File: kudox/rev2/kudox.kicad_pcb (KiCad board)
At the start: 2 copper layers, 143.6 x 129.5 mm, 83 parts, among them K0 KEYSW, K1 KEYSW, K10 KEYSW, K11 KEYSW, K12 KEYSW, K13 KEYSW, K14 KEYSW, K15 KEYSW, K16 KEYSW, K2 KEYSW, K20 KEYSW, K21 KEYSW, K22 KEYSW, K23 KEYSW, K24 KEYSW, K25 KEYSW, K3 KEYSW, K30 KEYSW, K31 KEYSW, K32 KEYSW, K33 KEYSW, K34 KEYSW, K35 KEYSW, K4 KEYSW, K40 KEYSW, K41 KEYSW, K42 KEYSW, K43 KEYSW, K44 KEYSW, K45 KEYSW, K46 KEYSW, K5 KEYSW, K6 KEYSW, U1 ProMicro

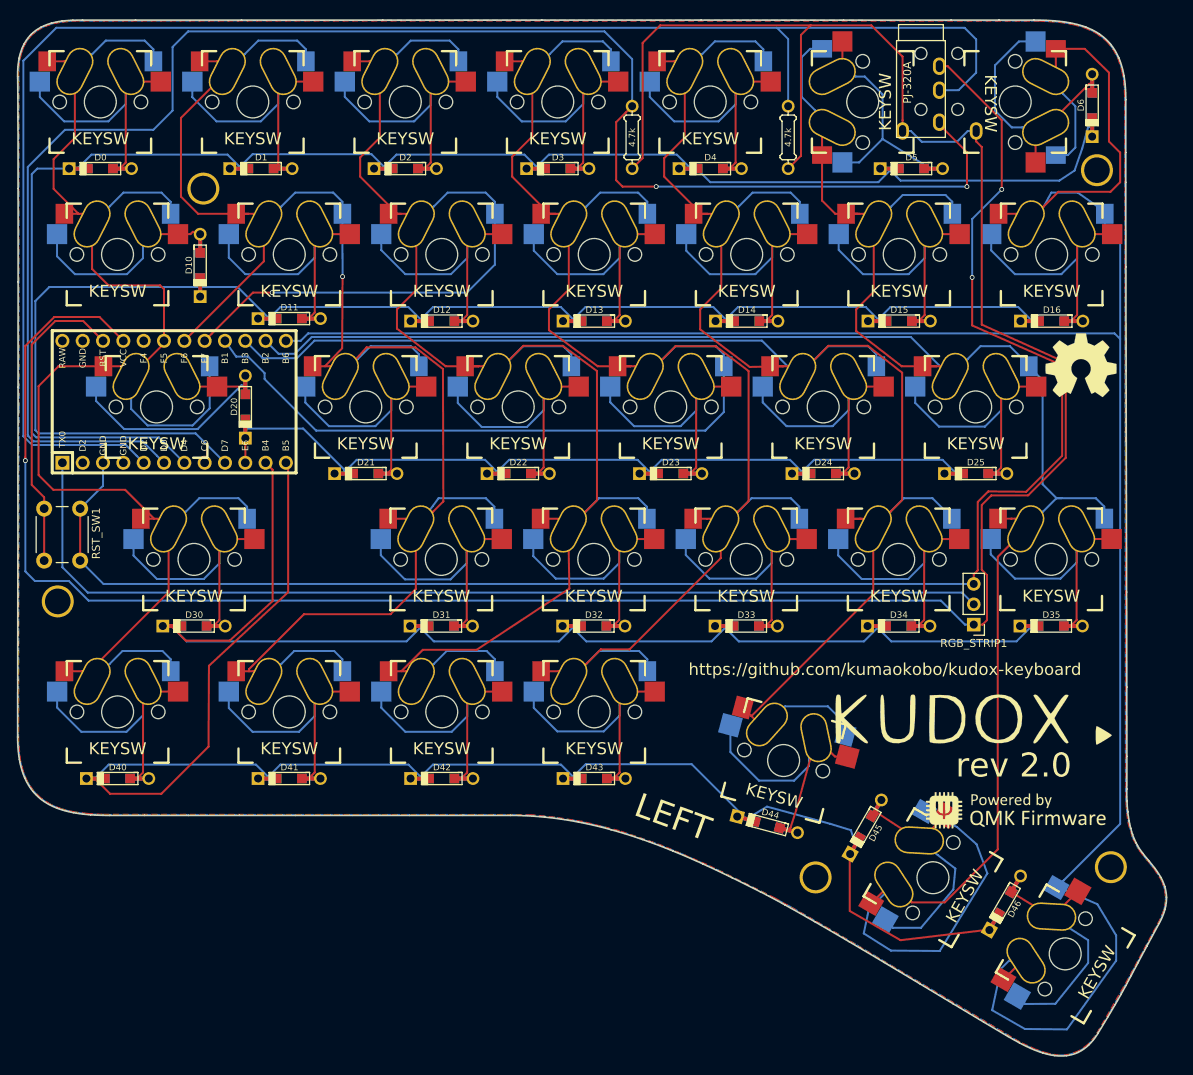
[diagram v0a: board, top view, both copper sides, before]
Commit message: Modified positions of holes.
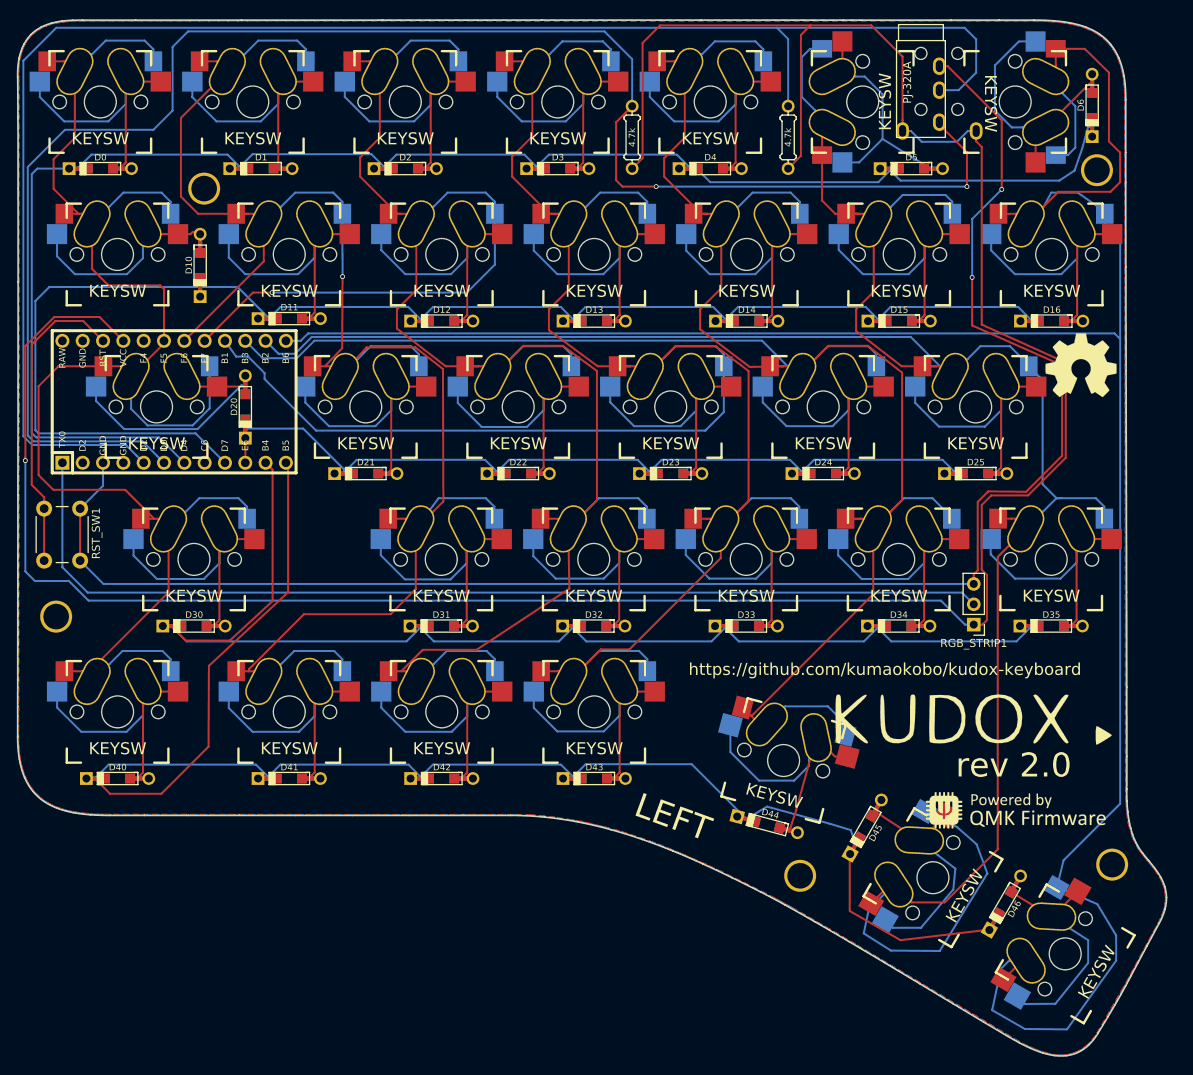
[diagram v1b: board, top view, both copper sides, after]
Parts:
- moved HOLE_M3 1.94 mm to (178.0, 138.4)
- moved HOLE_M3 1.91 mm to (85.0, 106.0)
- moved HOLE_M3 0.36 mm to (217.0, 137.0)
- moved HOLE_M3 0.10 mm to (103.5, 52.5)
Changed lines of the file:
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@@
     (thickness 1.6)
     (drawings 143)
-    (tracks 1082)
+    (tracks 1083)
     (zones 0)
     (modules 83)
@@
   )
   (module keyboard_parts:HOLE_M3 (layer F.Cu)
-    (at 179.93 138.56)
+    (at 178 138.36)
     (fp_text reference HOLE_M3 (at 0 -4.5) (layer F.SilkS) hide
       (effects (font (size 1.524 1.524) (thickness 0.3048)))
@@
   )
   (module keyboard_parts:HOLE_M3 (layer F.Cu)
-    (at 216.84 137.28)
+    (at 217 136.96)
     (fp_text reference HOLE_M3 (at 0 -4.5) (layer F.SilkS) hide
       (effects (font (size 1.524 1.524) (thickness 0.3048)))
@@
   )
   (module keyboard_parts:HOLE_M3 (layer F.Cu)
-    (at 103.4 52.46)
+    (at 103.5 52.46)
     (fp_text reference HOLE_M3 (at 0 -4.5) (layer F.SilkS) hide
       (effects (font (size 1.524 1.524) (thickness 0.3048)))
@@
   )
   (module keyboard_parts:HOLE_M3 (layer F.Cu)
-    (at 85.2 104.06)
+    (at 85 105.96)
     (fp_text reference HOLE_M3 (at -0.1 3.8) (layer F.SilkS) hide
       (effects (font (size 1.524 1.524) (thickness 0.3048)))
@@
   (gr_line (start 210.7 160.94) (end 237.7 160.94) (layer Dwgs.User) (width 0.1))
   (gr_line (start 60 31.36) (end 95 31.36) (layer Dwgs.User) (width 0.1))
-  (gr_line (start 59.99 130.84) (end 94.99 130.84) (layer Dwgs.User) (width 0.15))
+  (gr_line (start 59.99 130.84) (end 94.99 130.84) (layer Dwgs.User) (width 0.1))
   (gr_line (start 80.1 20.96) (end 80.1 165.86) (layer Dwgs.User) (width 0.1))
   (gr_line (start 223.85 21.04) (end 223.85 165.94) (layer Dwgs.User) (width 0.1))
@@
     (effects (font (size 3 3) (thickness 0.3)))
   )
-  (gr_curve (pts (xy 103.3398 50.856665) (xy 104.275584 50.856665) (xy 105.034187 51.615268) (xy 105.034187 52.551052)) (layer Eco1.User) (width 0.2))
+  (gr_curve (pts (xy 103.5098 50.766665) (xy 104.445584 50.766665) (xy 105.204187 51.525268) (xy 105.204187 52.461052)) (layer Eco1.User) (width 0.2))
   (gr_curve (pts (xy 213.413283 50.161035) (xy 213.413283 49.225251) (xy 214.171888 48.466648) (xy 215.107667 48.466648)) (layer Eco1.User) (width 0.2))
-  (gr_curve (pts (xy 85.195614 102.415616) (xy 86.131398 102.415616) (xy 86.89 103.174221) (xy 86.89 104.11)) (layer Eco1.User) (width 0.2))
-  (gr_curve (pts (xy 178.198782 138.530273) (xy 178.198782 137.594494) (xy 178.957386 136.835889) (xy 179.893166 136.835889)) (layer Eco1.User) (width 0.2))
-  (gr_curve (pts (xy 179.893166 140.224657) (xy 178.957386 140.224657) (xy 178.198782 139.466053) (xy 178.198782 138.530273)) (layer Eco1.User) (width 0.2))
-  (gr_curve (pts (xy 181.58755 138.530273) (xy 181.58755 139.466053) (xy 180.828945 140.224657) (xy 179.893166 140.224657)) (layer Eco1.User) (width 0.2))
-  (gr_curve (pts (xy 179.893166 136.835889) (xy 180.828945 136.835889) (xy 181.58755 137.594494) (xy 181.58755 138.530273)) (layer Eco1.User) (width 0.2))
-  (gr_curve (pts (xy 101.645414 52.551052) (xy 101.645414 51.615268) (xy 102.404017 50.856665) (xy 103.3398 50.856665)) (layer Eco1.User) (width 0.2))
-  (gr_curve (pts (xy 103.3398 54.245439) (xy 102.404017 54.245439) (xy 101.645414 53.486836) (xy 101.645414 52.551052)) (layer Eco1.User) (width 0.2))
-  (gr_curve (pts (xy 105.034187 52.551052) (xy 105.034187 53.486836) (xy 104.275584 54.245439) (xy 103.3398 54.245439)) (layer Eco1.User) (width 0.2))
+  (gr_curve (pts (xy 85.005614 104.265616) (xy 85.941398 104.265616) (xy 86.7 105.024221) (xy 86.7 105.96)) (layer Eco1.User) (width 0.2))
+  (gr_curve (pts (xy 176.298782 138.360273) (xy 176.298782 137.424494) (xy 177.057386 136.665889) (xy 177.993166 136.665889)) (layer Eco1.User) (width 0.2))
+  (gr_curve (pts (xy 177.993166 140.054657) (xy 177.057386 140.054657) (xy 176.298782 139.296053) (xy 176.298782 138.360273)) (layer Eco1.User) (width 0.2))
+  (gr_curve (pts (xy 179.68755 138.360273) (xy 179.68755 139.296053) (xy 178.928945 140.054657) (xy 177.993166 140.054657)) (layer Eco1.User) (width 0.2))
+  (gr_curve (pts (xy 177.993166 136.665889) (xy 178.928945 136.665889) (xy 179.68755 137.424494) (xy 179.68755 138.360273)) (layer Eco1.User) (width 0.2))
+  (gr_curve (pts (xy 101.815414 52.461052) (xy 101.815414 51.525268) (xy 102.574017 50.766665) (xy 103.5098 50.766665)) (layer Eco1.User) (width 0.2))
+  (gr_curve (pts (xy 103.5098 54.155439) (xy 102.574017 54.155439) (xy 101.815414 53.396836) (xy 101.815414 52.461052)) (layer Eco1.User) (width 0.2))
+  (gr_curve (pts (xy 105.204187 52.461052) (xy 105.204187 53.396836) (xy 104.445584 54.155439) (xy 103.5098 54.155439)) (layer Eco1.User) (width 0.2))
   (gr_curve (pts (xy 215.107667 51.855422) (xy 214.171888 51.855422) (xy 213.413283 51.096819) (xy 213.413283 50.161035)) (layer Eco1.User) (width 0.2))
   (gr_curve (pts (xy 216.802051 50.161035) (xy 216.802051 51.096819) (xy 216.043447 51.855422) (xy 215.107667 51.855422)) (layer Eco1.User) (width 0.2))
   (gr_curve (pts (xy 215.107667 48.466648) (xy 216.043447 48.466648) (xy 216.802051 49.225251) (xy 216.802051 50.161035)) (layer Eco1.User) (width 0.2))
-  (gr_curve (pts (xy 215.103649 137.155215) (xy 215.103649 136.219435) (xy 215.862253 135.460831) (xy 216.798033 135.460831)) (layer Eco1.User) (width 0.2))
-  (gr_curve (pts (xy 216.798033 138.849599) (xy 215.862253 138.849599) (xy 215.103649 138.090994) (xy 215.103649 137.155215)) (layer Eco1.User) (width 0.2))
-  (gr_curve (pts (xy 218.492417 137.155215) (xy 218.492417 138.090994) (xy 217.733812 138.849599) (xy 216.798033 138.849599)) (layer Eco1.User) (width 0.2))
-  (gr_curve (pts (xy 216.798033 135.460831) (xy 217.733812 135.460831) (xy 218.492417 136.219435) (xy 218.492417 137.155215)) (layer Eco1.User) (width 0.2))
-  (gr_curve (pts (xy 83.501227 104.11) (xy 83.501227 103.174221) (xy 84.259829 102.415616) (xy 85.195614 102.415616)) (layer Eco1.User) (width 0.2))
-  (gr_curve (pts (xy 85.195614 105.804384) (xy 84.259829 105.804384) (xy 83.501227 105.045779) (xy 83.501227 104.11)) (layer Eco1.User) (width 0.2))
-  (gr_curve (pts (xy 86.89 104.11) (xy 86.89 105.045779) (xy 86.131398 105.804384) (xy 85.195614 105.804384)) (layer Eco1.User) (width 0.2))
+  (gr_curve (pts (xy 215.303649 136.955215) (xy 215.303649 136.019435) (xy 216.062253 135.260831) (xy 216.998033 135.260831)) (layer Eco1.User) (width 0.2))
+  (gr_curve (pts (xy 216.998033 138.649599) (xy 216.062253 138.649599) (xy 215.303649 137.890994) (xy 215.303649 136.955215)) (layer Eco1.User) (width 0.2))
+  (gr_curve (pts (xy 218.692417 136.955215) (xy 218.692417 137.890994) (xy 217.933812 138.649599) (xy 216.998033 138.649599)) (layer Eco1.User) (width 0.2))
+  (gr_curve (pts (xy 216.998033 135.260831) (xy 217.933812 135.260831) (xy 218.692417 136.019435) (xy 218.692417 136.955215)) (layer Eco1.User) (width 0.2))
+  (gr_curve (pts (xy 83.311227 105.96) (xy 83.311227 105.024221) (xy 84.069829 104.265616) (xy 85.005614 104.265616)) (layer Eco1.User) (width 0.2))
+  (gr_curve (pts (xy 85.005614 107.654384) (xy 84.069829 107.654384) (xy 83.311227 106.895779) (xy 83.311227 105.96)) (layer Eco1.User) (width 0.2))
+  (gr_curve (pts (xy 86.7 105.96) (xy 86.7 106.895779) (xy 85.941398 107.654384) (xy 85.005614 107.654384)) (layer Eco1.User) (width 0.2))
   (gr_curve (pts (xy 87.095678 31.415371) (xy 87.524801 31.400242) (xy 87.933036 31.399453) (xy 88.305313 31.399453)) (layer Edge.Cuts) (width 0.2))
   (gr_curve (pts (xy 85.760717 31.517332) (xy 86.216544 31.45997) (xy 86.666555 31.430501) (xy 87.095678 31.415371)) (layer Edge.Cuts) (width 0.2))
@@
   (segment (start 216.08 57.11) (end 218 59.03) (width 0.25) (layer B.Cu) (net 44))
   (segment (start 216.08 55.61) (end 216.08 57.11) (width 0.25) (layer B.Cu) (net 44))
-  (segment (start 210.926556 138.953626) (end 210.050591 139.829591) (width 0.25) (layer B.Cu) (net 44))
-  (segment (start 218 131.880182) (end 210.926556 138.953626) (width 0.25) (layer B.Cu) (net 44))
   (segment (start 209.4 52.96) (end 208.438359 54.701641) (width 0.25) (layer B.Cu) (net 44))
   (segment (start 212.7 52.96) (end 209.4 52.96) (width 0.25) (layer B.Cu) (net 44))
@@
   (segment (start 212.4 47.33) (end 212.4 42.16) (width 0.25) (layer B.Cu) (net 44))
   (segment (start 209.96 48.27) (end 211.46 48.27) (width 0.25) (layer B.Cu) (net 44))
-  (segment (start 218 71.26) (end 218 131.880182) (width 0.25) (layer B.Cu) (net 44))
   (segment (start 218 59.03) (end 218 71.26) (width 0.25) (layer B.Cu) (net 44))
   (segment (start 217.3 70.56) (end 218 71.26) (width 0.25) (layer B.Cu) (net 44))
@@
   (segment (start 216.6 37.96) (end 216.6 46.56) (width 0.25) (layer F.Cu) (net 44))
   (segment (start 209.96 34.99) (end 213.58 34.99) (width 0.25) (layer F.Cu) (net 44))
+  (segment (start 210.3 138.96) (end 210.050591 139.829591) (width 0.25) (layer B.Cu) (net 44))
+  (segment (start 210.926556 136.433444) (end 210.3 138.96) (width 0.25) (layer B.Cu) (net 44))
+  (segment (start 218 129.36) (end 210.926556 136.433444) (width 0.25) (layer B.Cu) (net 44))
+  (segment (start 218 71.26) (end 218 129.36) (width 0.25) (layer B.Cu) (net 44))
   (segment (start 200.8 106.96) (end 199.7 106.96) (width 0.25) (layer F.Cu) (net 45))
   (segment (start 201.35 106.41) (end 200.8 106.96) (width 0.25) (layer F.Cu) (net 45))

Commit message: Modified drill aux.
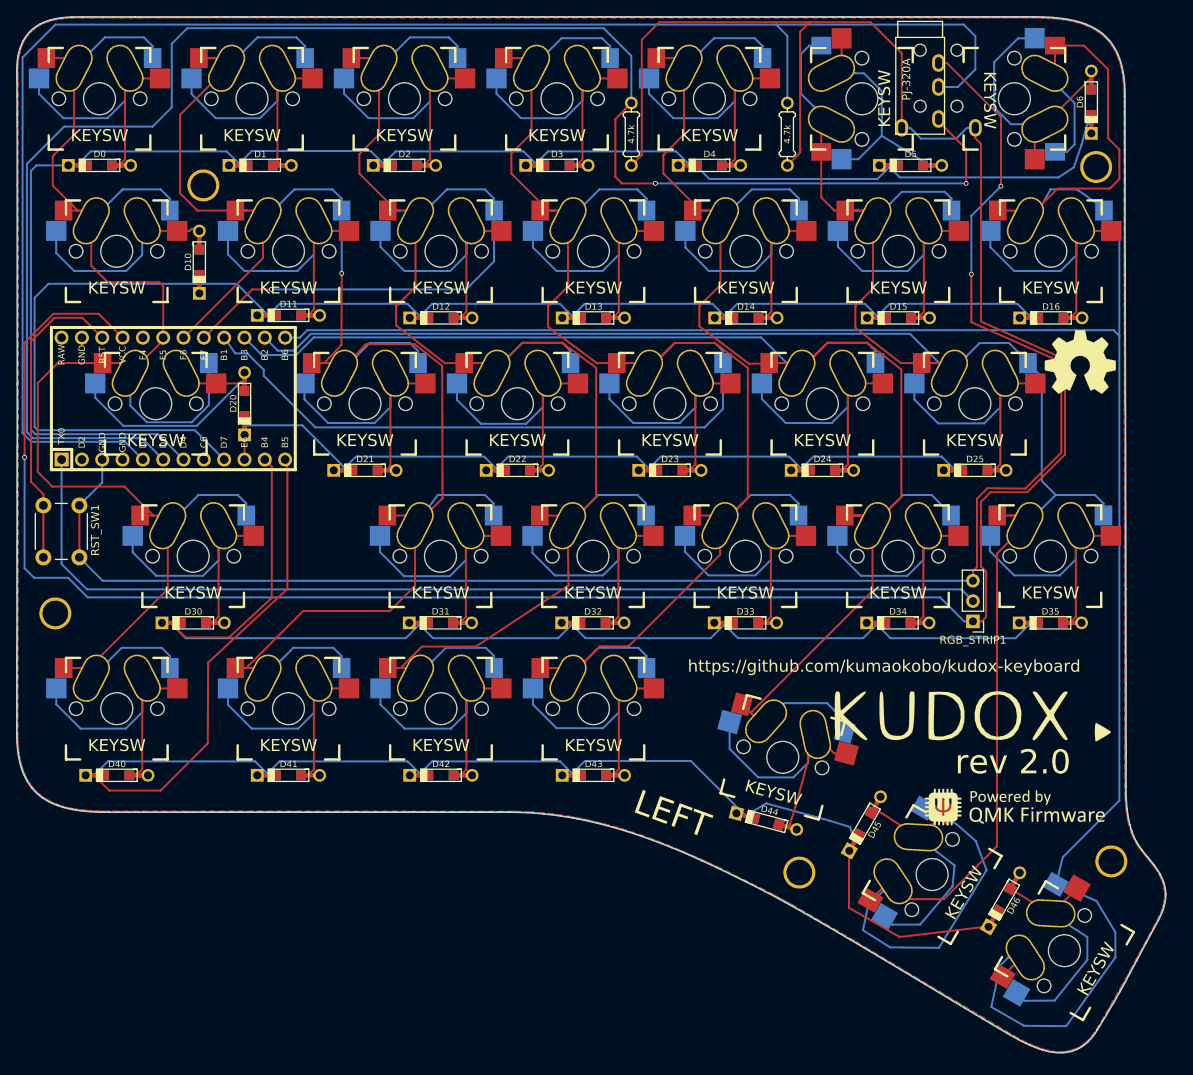
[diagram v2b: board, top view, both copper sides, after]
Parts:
- moved G*** 0.41 mm to (198.7, 118.5)
- moved D20 0.41 mm to (108.5, 79.3)
- moved D30 0.41 mm to (102.1, 106.7)
- moved D40 0.41 mm to (92.6, 125.8)
- moved K21 0.41 mm to (123.6, 79.3)
- moved K30 0.41 mm to (102.1, 98.4)
- moved K40 0.41 mm to (92.6, 117.5)
- moved -3 0.41 mm to (213.0, 74.2)
- moved D10 0.41 mm to (102.9, 61.7)
- moved D31 0.41 mm to (133.0, 106.7)
- moved D32 0.41 mm to (152.1, 106.7)
- moved D33 0.41 mm to (171.2, 106.7)
- moved D34 0.41 mm to (190.2, 106.7)
- moved D35 0.41 mm to (209.3, 106.7)
- moved D41 0.41 mm to (114.0, 125.8)
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
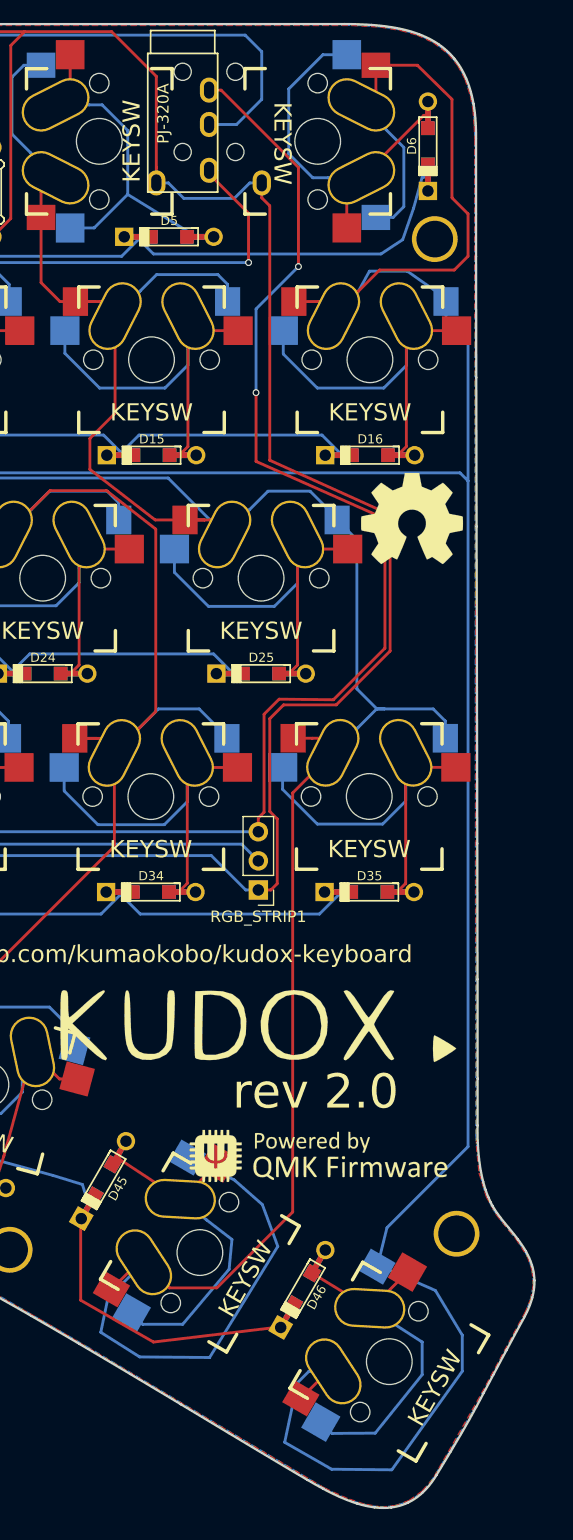
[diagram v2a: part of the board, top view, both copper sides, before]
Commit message: Modified the direction of switches on 6th row.
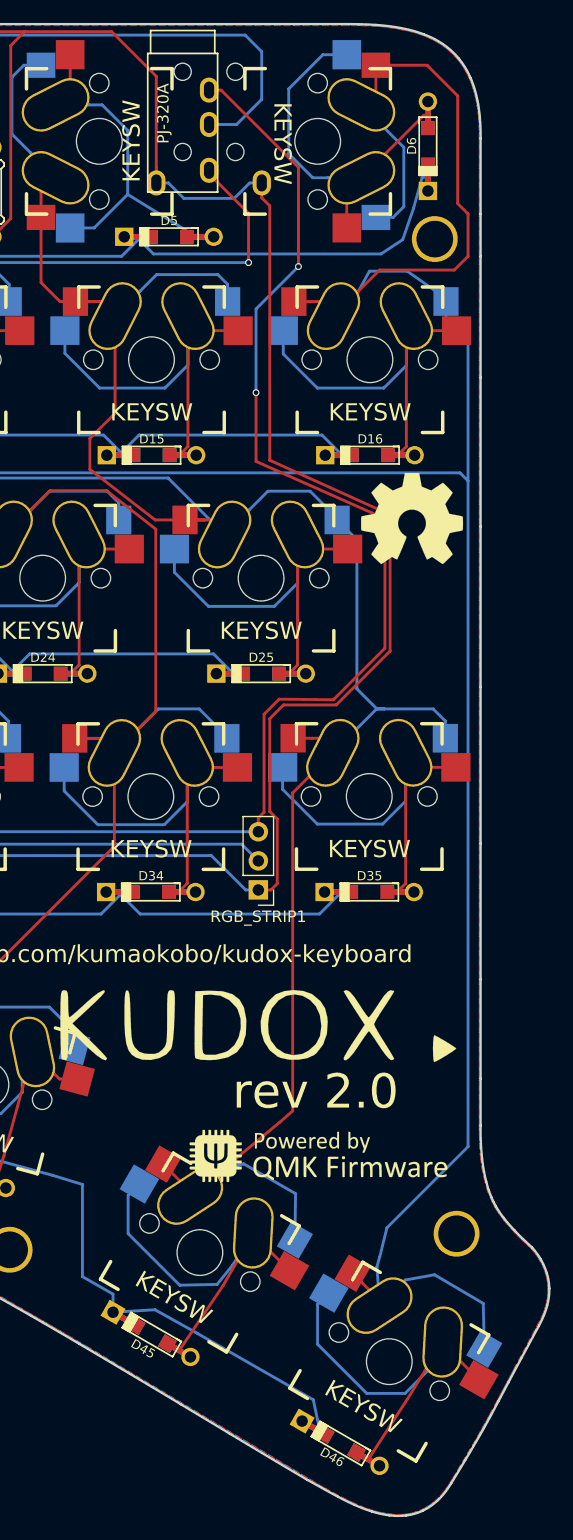
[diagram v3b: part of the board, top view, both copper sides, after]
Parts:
- moved D45 14.1 mm to (190.3, 145.4), turned to 150 degrees
- moved D46 13.9 mm to (206.8, 154.9), turned to 150 degrees
- turned K45 to 330 degrees
- turned K46 to 330 degrees
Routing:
- net col5: track 317.1 -> 276.6 mm
- net col6: track 309.5 -> 285.5 mm
- net Net-(D45-Pad2): track 31.0 -> 36.6 mm
- net row4: track 200.9 -> 206.3 mm
- net Net-(D46-Pad2): track 32.8 -> 36.9 mm
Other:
- board size 143.6 x 129.5 mm -> 144.9 x 130.2 mm
